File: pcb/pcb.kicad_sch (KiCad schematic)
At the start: 27 parts, among them J1 Screw_Terminal_01x02, J2 Screw_Terminal_01x04, J3 Screw_Terminal_01x04, J4 Screw_Terminal_01x03, J5 Screw_Terminal_01x06, Q1 2N7000, Q2 2N7000, Q3 2N7000

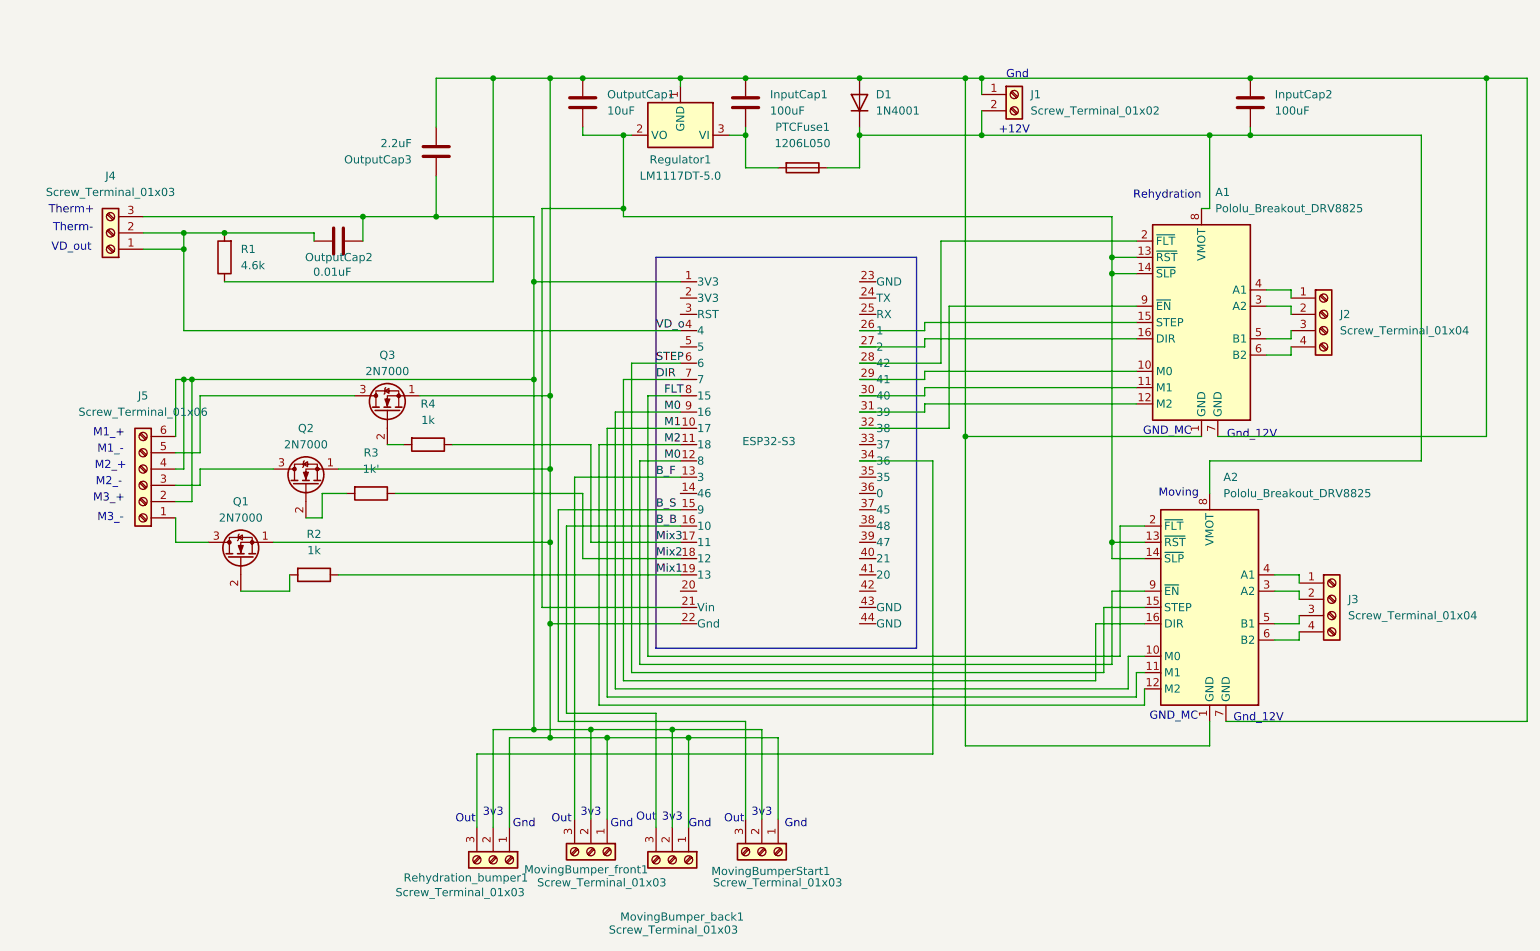
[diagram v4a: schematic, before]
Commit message: mixing controllers to 12V and add extra screw terminal for heating control
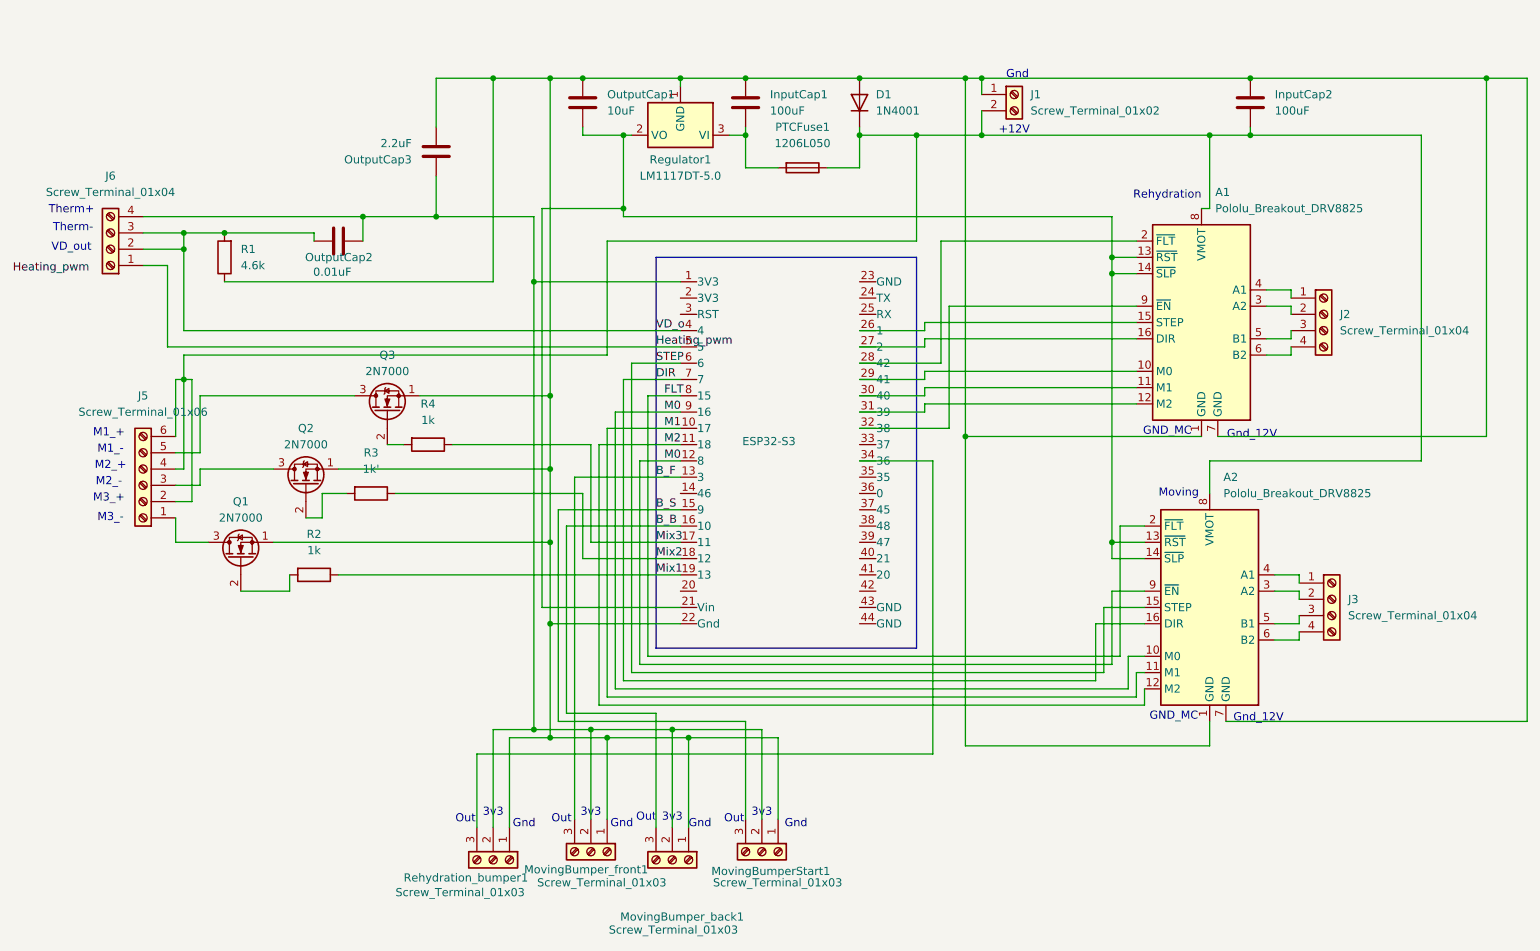
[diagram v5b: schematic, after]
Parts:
- removed J4: Screw_Terminal_01x03, TerminalBlock:TerminalBlock_MaiXu_MX126-5.0-03P_1x03_P5.00mm, symbol Connector:Screw_Terminal_01x03
- added J6: Screw_Terminal_01x04, symbol Connector:Screw_Terminal_01x04
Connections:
- net VD_o: now also J6.2 (Pin_2), J6.3 (Pin_3)
- net at ESP32-S3.1 (3V3), MovingBumperStart1.2 (Pin_2), MovingBumper_back1.2 (Pin_2)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: now also J6.4 (Pin_4); no longer J5.2 (Pin_2), J5.4 (Pin_4), J5.6 (Pin_6)
- net Heating_pwm: now reaches ESP32-S3.5
- net Heating_pwm: now also J6.1 (Pin_1)
- net at A1.8 (VMOT), A2.8 (VMOT), D1.1 (K)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: now also J5.2 (Pin_2), J5.4 (Pin_4), J5.6 (Pin_6)
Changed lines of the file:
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@@
 	)
 	(junction
+		(at 67.31 71.12)
+		(diameter 0)
+		(color 0 0 0 0)
+	)
+	(junction
 		(at 67.31 48.26)
 		(diameter 0)
@@
 	)
 	(junction
+		(at 181.61 33.02)
+		(diameter 0)
+		(color 0 0 0 0)
+	)
+	(junction
 		(at 67.31 50.8)
 		(diameter 0)
@@
 	)
 	(junction
-		(at 68.58 71.12)
-		(diameter 0)
-		(color 0 0 0 0)
-	)
-	(junction
 		(at 130.81 125.73)
 		(diameter 0)
@@
 	)
 	(junction
-		(at 121.92 71.12)
-		(diameter 0)
-		(color 0 0 0 0)
-	)
-	(junction
 		(at 270.51 24.13)
 		(diameter 0)
@@
 	)
 	(junction
-		(at 67.31 71.12)
-		(diameter 0)
-		(color 0 0 0 0)
-	)
-	(junction
 		(at 212.09 96.52)
 		(diameter 0)
@@
 	(wire
 		(pts
-			(xy 68.58 71.12) (xy 121.92 71.12)
+			(xy 64.77 53.34) (xy 64.77 66.04)
 		)
 		(stroke
@@
 	(wire
 		(pts
+			(xy 67.31 67.31) (xy 133.35 67.31)
+		)
+		(stroke
+			(width 0)
+			(type default)
+		)
+	)
+	(wire
+		(pts
 			(xy 129.54 24.13) (xy 144.78 24.13)
 		)
@@
 	(wire
 		(pts
+			(xy 67.31 71.12) (xy 67.31 67.31)
+		)
+		(stroke
+			(width 0)
+			(type default)
+		)
+	)
+	(wire
+		(pts
 			(xy 124.46 127) (xy 124.46 109.22)
 		)
@@
 	(wire
 		(pts
+			(xy 60.96 53.34) (xy 64.77 53.34)
+		)
+		(stroke
+			(width 0)
+			(type default)
+		)
+	)
+	(wire
+		(pts
 			(xy 209.55 109.22) (xy 209.55 118.11)
 		)
@@
 	(wire
 		(pts
+			(xy 64.77 66.04) (xy 144.78 66.04)
+		)
+		(stroke
+			(width 0)
+			(type default)
+		)
+	)
+	(wire
+		(pts
 			(xy 215.9 49.53) (xy 185.42 49.53)
 		)
@@
 	(wire
 		(pts
+			(xy 133.35 49.53) (xy 181.61 49.53)
+		)
+		(stroke
+			(width 0)
+			(type default)
+		)
+	)
+	(wire
+		(pts
 			(xy 67.31 48.26) (xy 73.66 48.26)
 		)
@@
 	(wire
 		(pts
-			(xy 121.92 55.88) (xy 121.92 71.12)
-		)
-		(stroke
-			(width 0)
-			(type default)
-		)
-	)
-	(wire
-		(pts
 			(xy 130.81 139.7) (xy 130.81 125.73)
 		)
@@
 	(wire
 		(pts
-			(xy 172.72 33.02) (xy 191.77 33.02)
+			(xy 172.72 33.02) (xy 181.61 33.02)
 		)
 		(stroke
@@
 	(wire
 		(pts
-			(xy 66.04 71.12) (xy 67.31 71.12)
-		)
-		(stroke
-			(width 0)
-			(type default)
-		)
-	)
-	(wire
-		(pts
 			(xy 227.33 83.82) (xy 260.35 83.82)
 		)
@@
 	(wire
 		(pts
+			(xy 67.31 71.12) (xy 68.58 71.12)
+		)
+		(stroke
+			(width 0)
+			(type default)
+		)
+	)
+	(wire
+		(pts
 			(xy 191.77 24.13) (xy 191.77 26.67)
 		)
@@
 	(wire
 		(pts
-			(xy 67.31 71.12) (xy 68.58 71.12)
+			(xy 66.04 71.12) (xy 67.31 71.12)
 		)
 		(stroke
@@
 	(wire
 		(pts
-			(xy 121.92 71.12) (xy 121.92 125.73)
+			(xy 121.92 55.88) (xy 121.92 125.73)
 		)
 		(stroke
@@
 	(wire
 		(pts
+			(xy 181.61 33.02) (xy 191.77 33.02)
+		)
+		(stroke
+			(width 0)
+			(type default)
+		)
+	)
+	(wire
+		(pts
 			(xy 260.35 33.02) (xy 233.68 33.02)
 		)
@@
 	(wire
 		(pts
+			(xy 181.61 49.53) (xy 181.61 33.02)
+		)
+		(stroke
+			(width 0)
+			(type default)
+		)
+	)
+	(wire
+		(pts
 			(xy 233.68 24.13) (xy 270.51 24.13)
 		)
@@
 		)
 	)
+	(wire
+		(pts
+			(xy 133.35 67.31) (xy 133.35 49.53)
+		)
+		(stroke
+			(width 0)
+			(type default)
+		)
+	)
 	(label "Mix2"
 		(at 140.97 99.06 0)
@@
 		)
 	)
+	(label "Heating_pwm"
+		(at 40.64 54.61 0)
+		(effects
+			(font
+				(size 1.27 1.27)
+			)
+			(justify left bottom)
+		)
+	)
 	(label "M0"
 		(at 142.24 76.2 0)
@@
 		)
 	)
+	(label "Heating_pwm"
+		(at 140.97 66.04 0)
+		(effects
+			(font
+				(size 1.27 1.27)
+			)
+			(justify left bottom)
+		)
+	)
 	(label "VD_o"
 		(at 140.97 63.5 0)
@@
 	)
 	(symbol
+		(lib_id "Connector:Screw_Terminal_01x04")
+		(at 55.88 50.8 180)
+		(unit 1)
+		(exclude_from_sim no)
+		(in_bom yes)
+		(on_board yes)
+		(dnp no)
+		(fields_autoplaced yes)
+		(property "Reference" "J6"
+			(at 55.88 39.37 0)
+			(effects
+				(font
+					(size 1.27 1.27)
+				)
+			)
+		)
+		(property "Value" "Screw_Terminal_01x04"
+			(at 55.88 41.91 0)
+			(effects
+				(font
+					(size 1.27 1.27)
+				)
+			)
+		)
+		(property "Footprint" ""
+			(at 55.88 50.8 0)
+			(effects
+				(font
+					(size 1.27 1.27)
+				)
+				(hide yes)
+			)
+		)
+		(property "Datasheet" "~"
+			(at 55.88 50.8 0)
+			(effects
+				(font
+					(size 1.27 1.27)
+				)
+				(hide yes)
+			)
+		)
+		(property "Description" "Generic screw terminal, single row, 01x04, script generated (kicad-library-utils/schlib/autogen/connector/)"
+			(at 55.88 50.8 0)
+			(effects
+				(font
+					(size 1.27 1.27)
+				)
+				(hide yes)
+			)
+		)
+		(pin "3"
+		)
+		(pin "1"
+		)
+		(pin "2"
+		)
+		(pin "4"
+		)
+		(instances
+			(project ""
+				(path "/5b8f4b4b-fd94-4673-8b66-f0a593fc8259"
+					(reference "J6")
+					(unit 1)
+				)
+			)
+		)
+	)
+	(symbol
 		(lib_id "Driver_Motor:Pololu_Breakout_DRV8825")
 		(at 227.33 104.14 0)
@@
 					(unit 1)
 				)
-			)
-		)
-	)
-	(symbol
-		(lib_id "Connector:Screw_Terminal_01x03")
-		(at 55.88 48.26 180)
-		(unit 1)
-		(exclude_from_sim no)
-		(in_bom yes)
-		(on_board yes)
-		(dnp no)
-		(fields_autoplaced yes)
-		(property "Reference" "J4"
-			(at 55.88 39.37 0)
-			(effects
-				(font
-					(size 1.27 1.27)
-				)
-			)
-		)
-		(property "Value" "Screw_Terminal_01x03"
-			(at 55.88 41.91 0)
-			(effects
-				(font
-					(size 1.27 1.27)
-				)
-			)
-		)
-		(property "Footprint" "TerminalBlock:TerminalBlock_MaiXu_MX126-5.0-03P_1x03_P5.00mm"
-			(at 55.88 48.26 0)
-			(effects
-				(font
-					(size 1.27 1.27)
-				)
-				(hide yes)
-			)
-		)
-		(property "Datasheet" "~"
-			(at 55.88 48.26 0)
-			(effects
-				(font
-					(size 1.27 1.27)
-				)
-				(hide yes)
-			)
-		)
-		(property "Description" "Generic screw terminal, single row, 01x03, script generated (kicad-library-utils/schlib/autogen/connector/)"
-			(at 55.88 48.26 0)
-			(effects
-				(font
-					(size 1.27 1.27)
-				)
-				(hide yes)
-			)
-		)
-		(pin "2"
-		)
-		(pin "1"
-		)
-		(pin "3"
-		)
-		(instances
-			(project ""
-				(path "/5b8f4b4b-fd94-4673-8b66-f0a593fc8259"
-					(reference "J4")
-					(unit 1)
-				)

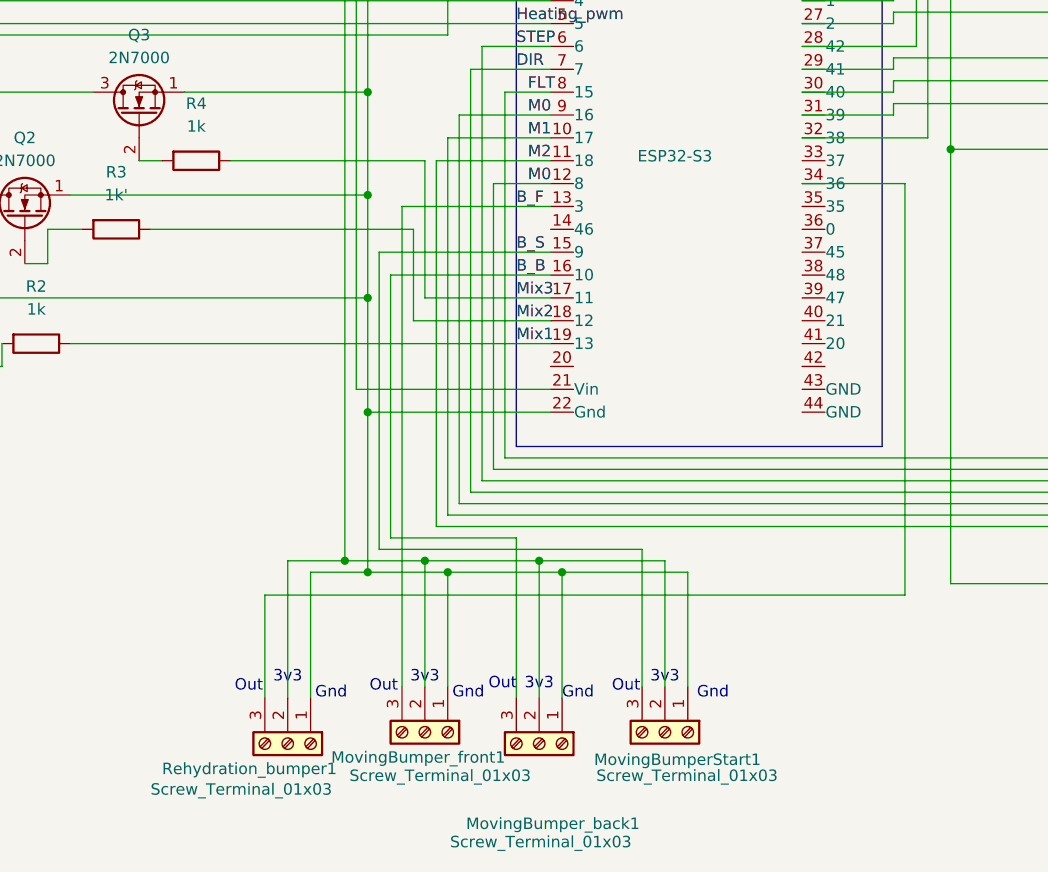
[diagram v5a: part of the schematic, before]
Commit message: changed names for moving bumper_start to rehydration back
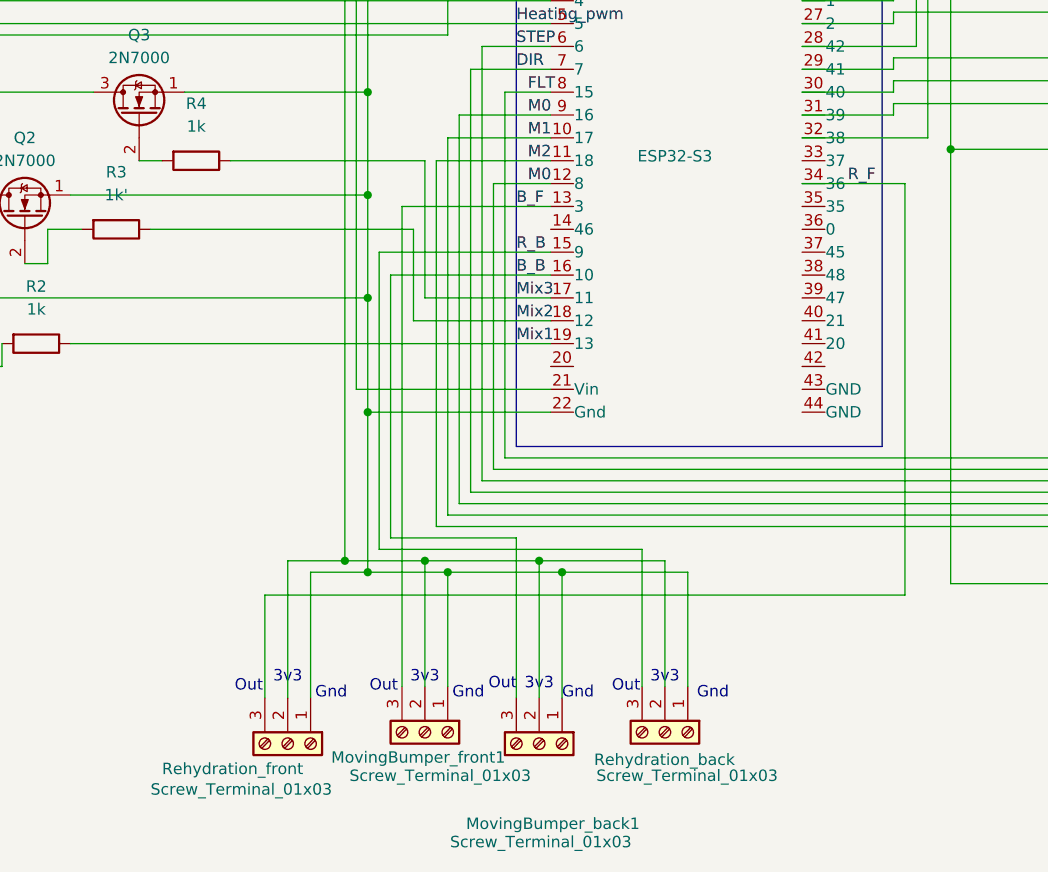
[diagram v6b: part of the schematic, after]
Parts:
- renumbered MovingBumperStart1 to Rehydration_back, Rehydration_bumper1 to Rehydration_front
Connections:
- net R_F: now reaches ESP32-S3.34 (36), Rehydration_front.3 (Pin_3)
- net B_S renamed R_B
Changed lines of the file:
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@@
+		)
+	)
+	(label "R_F"
+		(at 177.8 83.82 0)
+		(effects
+			(font
+				(size 1.27 1.27)
+			)
+			(justify left bottom)
 		)
 	)
@@
 		)
 	)
-	(label "B_S"
+	(label "R_B"
 		(at 140.97 91.44 0)
 		(effects
@@
 		(on_board yes)
 		(dnp no)
-		(property "Reference" "Rehydration_bumper1"
+		(property "Reference" "Rehydration_front"
 			(at 101.6 148.844 90)
 			(effects
@@
 			(project ""
 				(path "/5b8f4b4b-fd94-4673-8b66-f0a593fc8259"
-					(reference "Rehydration_bumper1")
+					(reference "Rehydration_front")
 					(unit 1)
 				)
@@
 		(on_board yes)
 		(dnp no)
-		(property "Reference" "MovingBumperStart1"
+		(property "Reference" "Rehydration_back"
 			(at 149.606 147.828 90)
 			(effects
@@
 			(project "pcb"
 				(path "/5b8f4b4b-fd94-4673-8b66-f0a593fc8259"
-					(reference "MovingBumperStart1")
+					(reference "Rehydration_back")
 					(unit 1)
 				)

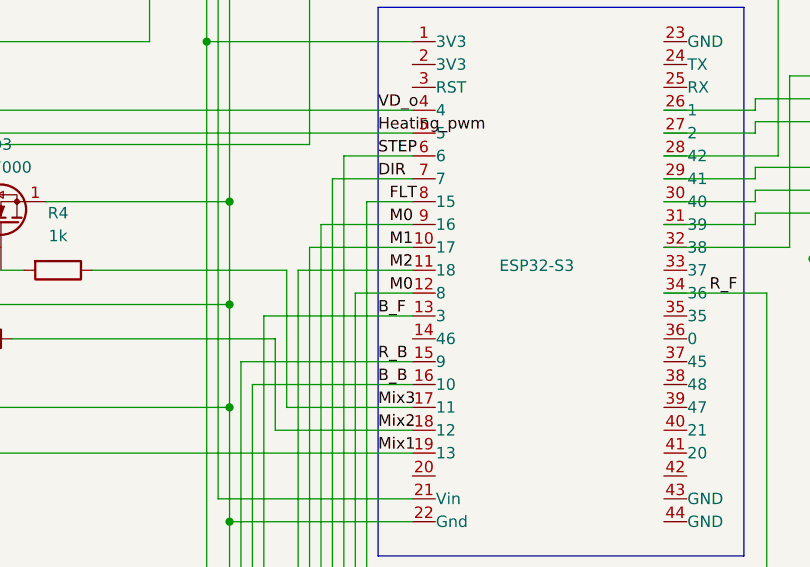
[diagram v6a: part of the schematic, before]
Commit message: changed name for M0 to En, had 2 M0's
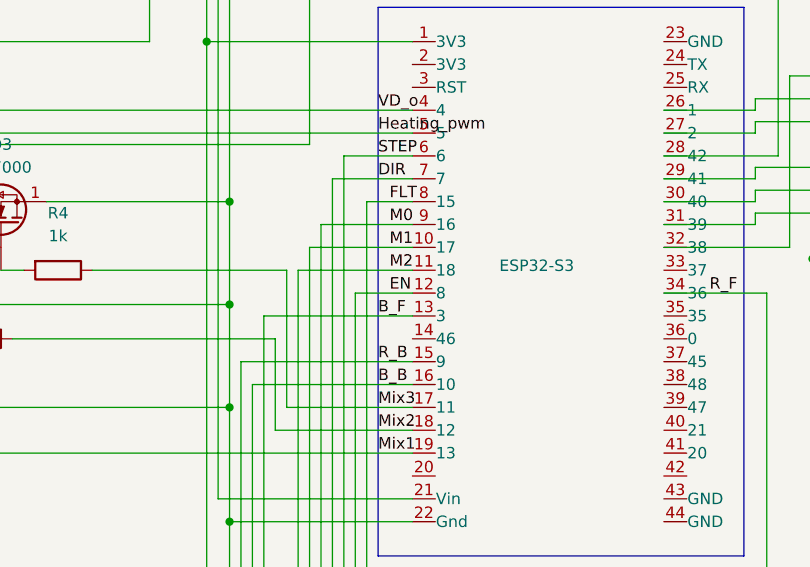
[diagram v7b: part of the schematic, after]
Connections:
- net M0: no longer A2.9 (~{EN}), ESP32-S3.12 (8)
- new net EN: A2.9 (~{EN}), ESP32-S3.12 (8)
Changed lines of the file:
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@@
 		)
 	)
-	(label "M0"
+	(label "EN"
 		(at 142.24 83.82 0)
 		(effects
